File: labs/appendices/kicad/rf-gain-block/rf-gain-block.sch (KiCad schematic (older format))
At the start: 10 parts, among them P1 SMA, P2 SMA, P3 CONN_01X02, U1 ADL5602

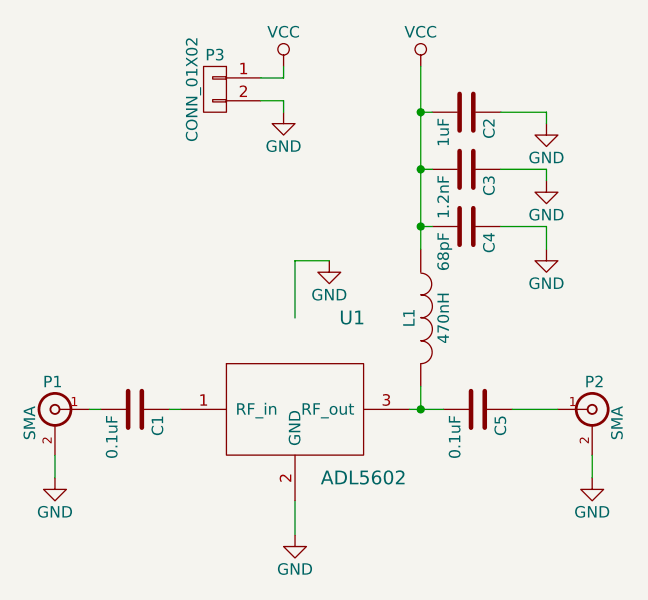
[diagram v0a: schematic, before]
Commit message: update pcb tutorial
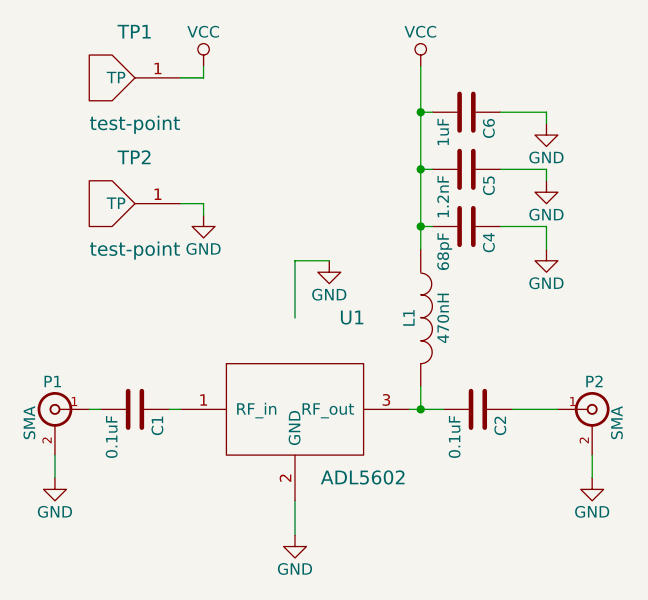
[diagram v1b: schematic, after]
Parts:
- removed P3: CONN_01X02, Pin_Headers:Pin_Header_Straight_1x02, symbol CONN_01X02
- added TP1, TP2: test-point, rf-gain-block-footprints:tp, symbol test-point
- C1, C4: footprint Capacitors_SMD:C_0402 -> rf-gain-block-footprints:smd_0603
- C2: renamed from C5; footprint Capacitors_SMD:C_0402 -> rf-gain-block-footprints:smd_0603
- C5: renamed from C3; footprint Capacitors_SMD:C_0402 -> rf-gain-block-footprints:smd_0603
- C6: renamed from C2; footprint Capacitors_SMD:C_0402 -> rf-gain-block-footprints:smd_0603
- L1: footprint (none) -> rf-gain-block-footprints:cc_0603ls
- P1, P2: footprint (none) -> rf-gain-block-footprints:SMA
- U1: footprint (none) -> rf-gain-block-footprints:adl5602
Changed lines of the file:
@@
 $EndDescr
 $Comp
-L GND #PWR4
+L GND #PWR01
 U 1 1 55D2CC7E
 P 5400 4200
-F 0 "#PWR4" H 5400 3950 50  0001 C CNN
+F 0 "#PWR01" H 5400 3950 50  0001 C CNN
 F 1 "GND" H 5400 4050 50  0000 C CNN
 F 2 "" H 5400 4200 60  0000 C CNN
@@
 F 0 "U1" H 5650 4050 60  0000 C CNN
 F 1 "ADL5602" H 5700 3350 60  0000 C CNN
-F 2 "" H 5400 3650 60  0001 C CNN
+F 2 "rf-gain-block-footprints:adl5602" H 5400 3650 60  0001 C CNN
 F 3 "" H 5400 3650 60  0000 C CNN
 	1    5400 3650
@@
 F 0 "P2" H 6710 3770 50  0000 C CNN
 F 1 "SMA" V 6810 3590 50  0000 C CNN
-F 2 "" H 6700 3650 60  0001 C CNN
+F 2 "rf-gain-block-footprints:SMA" H 6700 3650 60  0001 C CNN
 F 3 "" H 6700 3650 60  0000 C CNN
 	1    6700 3650
@@
 F 0 "P1" H 4360 3770 50  0000 C CNN
 F 1 "SMA" V 4460 3590 50  0000 C CNN
-F 2 "" H 4350 3650 60  0001 C CNN
+F 2 "rf-gain-block-footprints:SMA" H 4350 3650 60  0001 C CNN
 F 3 "" H 4350 3650 60  0000 C CNN
 	1    4350 3650
@@
 	6350 3650 6550 3650
 $Comp
-L GND #PWR10
+L GND #PWR02
 U 1 1 55D2D10F
 P 6700 3950
-F 0 "#PWR10" H 6700 3700 50  0001 C CNN
+F 0 "#PWR02" H 6700 3700 50  0001 C CNN
 F 1 "GND" H 6700 3800 50  0000 C CNN
 F 2 "" H 6700 3950 60  0000 C CNN
@@
 $EndComp
 $Comp
-L GND #PWR5
+L GND #PWR03
 U 1 1 55D2D123
 P 5550 3000
-F 0 "#PWR5" H 5550 2750 50  0001 C CNN
+F 0 "#PWR03" H 5550 2750 50  0001 C CNN
 F 1 "GND" H 5550 2850 50  0000 C CNN
 F 2 "" H 5550 3000 60  0000 C CNN
@@
 $EndComp
 $Comp
-L GND #PWR1
+L GND #PWR04
 U 1 1 55D2D137
 P 4350 3950
-F 0 "#PWR1" H 4350 3700 50  0001 C CNN
+F 0 "#PWR04" H 4350 3700 50  0001 C CNN
 F 1 "GND" H 4350 3800 50  0000 C CNN
 F 2 "" H 4350 3950 60  0000 C CNN
@@
 F 0 "C1" H 4725 3750 50  0000 L CNN
 F 1 "0.1uF" H 4725 3550 50  0000 L CNN
-F 2 "Capacitors_SMD:C_0402" H 4738 3500 30  0001 C CNN
+F 2 "rf-gain-block-footprints:smd_0603" H 4738 3500 30  0001 C CNN
 F 3 "" H 4700 3650 60  0000 C CNN
 	1    4700 3650
@@
 $EndComp
 $Comp
-L C C3
+L C C5
 U 1 1 55D2D1D7
 P 6150 2600
-F 0 "C3" H 6175 2700 50  0000 L CNN
+F 0 "C5" H 6175 2700 50  0000 L CNN
 F 1 "1.2nF" H 6175 2500 50  0000 L CNN
-F 2 "Capacitors_SMD:C_0402" H 6188 2450 30  0001 C CNN
+F 2 "rf-gain-block-footprints:smd_0603" H 6188 2450 30  0001 C CNN
 F 3 "" H 6150 2600 60  0000 C CNN
 	1    6150 2600
@@
 F 0 "C4" H 6175 2950 50  0000 L CNN
 F 1 "68pF" H 6175 2750 50  0000 L CNN
-F 2 "Capacitors_SMD:C_0402" H 6188 2700 30  0001 C CNN
+F 2 "rf-gain-block-footprints:smd_0603" H 6188 2700 30  0001 C CNN
 F 3 "" H 6150 2850 60  0000 C CNN
 	1    6150 2850
@@
 $EndComp
 $Comp
-L C C2
+L C C6
 U 1 1 55D2D25D
 P 6150 2350
-F 0 "C2" H 6175 2450 50  0000 L CNN
+F 0 "C6" H 6175 2450 50  0000 L CNN
 F 1 "1uF" H 6175 2250 50  0000 L CNN
-F 2 "Capacitors_SMD:C_0402" H 6188 2200 30  0001 C CNN
+F 2 "rf-gain-block-footprints:smd_0603" H 6188 2200 30  0001 C CNN
 F 3 "" H 6150 2350 60  0000 C CNN
 	1    6150 2350
@@
 F 0 "L1" V 5900 3250 50  0000 C CNN
 F 1 "470nH" V 6050 3250 50  0000 C CNN
-F 2 "" H 5950 3250 60  0001 C CNN
+F 2 "rf-gain-block-footprints:cc_0603ls" H 5950 3250 60  0001 C CNN
 F 3 "" H 5950 3250 60  0000 C CNN
 	1    5950 3250
@@
 $EndComp
 $Comp
-L C C5
+L C C2
 U 1 1 55D2D3C6
 P 6200 3650
-F 0 "C5" H 6225 3750 50  0000 L CNN
+F 0 "C2" H 6225 3750 50  0000 L CNN
 F 1 "0.1uF" H 6225 3550 50  0000 L CNN
-F 2 "Capacitors_SMD:C_0402" H 6238 3500 30  0001 C CNN
+F 2 "rf-gain-block-footprints:smd_0603" H 6238 3500 30  0001 C CNN
 F 3 "" H 6200 3650 60  0000 C CNN
 	1    6200 3650
@@
 	4550 3650 4500 3650
 Wire Wire Line
-	6000 2850 5950 2850
+	5950 2850 6000 2850
 Wire Wire Line
 	5950 2150 5950 2950
@@
 Connection ~ 5950 2600
 $Comp
-L GND #PWR9
+L GND #PWR05
 U 1 1 55D2D53E
 P 6500 2950
-F 0 "#PWR9" H 6500 2700 50  0001 C CNN
+F 0 "#PWR05" H 6500 2700 50  0001 C CNN
 F 1 "GND" H 6500 2800 50  0000 C CNN
 F 2 "" H 6500 2950 60  0000 C CNN
@@
 $EndComp
 $Comp
-L GND #PWR8
+L GND #PWR06
 U 1 1 55D2D576
 P 6500 2650
-F 0 "#PWR8" H 6500 2400 50  0001 C CNN
+F 0 "#PWR06" H 6500 2400 50  0001 C CNN
 F 1 "GND" H 6500 2500 50  0000 C CNN
 F 2 "" H 6500 2650 60  0000 C CNN
@@
 $EndComp
 $Comp
-L GND #PWR7
+L GND #PWR07
 U 1 1 55D2D59C
 P 6500 2400
-F 0 "#PWR7" H 6500 2150 50  0001 C CNN
+F 0 "#PWR07" H 6500 2150 50  0001 C CNN
 F 1 "GND" H 6500 2250 50  0000 C CNN
 F 2 "" H 6500 2400 60  0000 C CNN
@@
 	6500 2850 6500 2950
 $Comp
-L VCC #PWR6
+L VCC #PWR08
 U 1 1 55D2D630
 P 5950 2150
-F 0 "#PWR6" H 5950 2000 50  0001 C CNN
+F 0 "#PWR08" H 5950 2000 50  0001 C CNN
 F 1 "VCC" H 5950 2300 50  0000 C CNN
 F 2 "" H 5950 2150 60  0000 C CNN
@@
 Connection ~ 5950 2350
 $Comp
-L CONN_01X02 P3
-U 1 1 55D2DB86
-P 5050 2250
-F 0 "P3" H 5050 2400 50  0000 C CNN
-F 1 "CONN_01X02" V 5150 2250 50  0000 C CNN
-F 2 "Pin_Headers:Pin_Header_Straight_1x02" H 5050 2250 60  0001 C CNN
-F 3 "" H 5050 2250 60  0000 C CNN
-	1    5050 2250
-	-1   0    0    -1
-$EndComp
-$Comp
-L VCC #PWR2
+L VCC #PWR09
 U 1 1 55D2DC4B
-P 5350 2150
-F 0 "#PWR2" H 5350 2000 50  0001 C CNN
-F 1 "VCC" H 5350 2300 50  0000 C CNN
-F 2 "" H 5350 2150 60  0000 C CNN
-F 3 "" H 5350 2150 60  0000 C CNN
-	1    5350 2150
-	1    0    0    -1
-$EndComp
-$Comp
-L GND #PWR3
+P 5000 2150
+F 0 "#PWR09" H 5000 2000 50  0001 C CNN
+F 1 "VCC" H 5000 2300 50  0000 C CNN
+F 2 "" H 5000 2150 60  0000 C CNN
+F 3 "" H 5000 2150 60  0000 C CNN
+	1    5000 2150
+	1    0    0    -1
+$EndComp
+$Comp
+L GND #PWR010
 U 1 1 55D2DC73
-P 5350 2350
-F 0 "#PWR3" H 5350 2100 50  0001 C CNN
-F 1 "GND" H 5350 2200 50  0000 C CNN
-F 2 "" H 5350 2350 60  0000 C CNN
-F 3 "" H 5350 2350 60  0000 C CNN
-	1    5350 2350
-	1    0    0    -1
-$EndComp
-Wire Wire Line
-	5350 2150 5350 2200
-Wire Wire Line
-	5350 2200 5250 2200
-Wire Wire Line
-	5250 2300 5350 2300
-Wire Wire Line
-	5350 2300 5350 2350
+P 5000 2800
+F 0 "#PWR010" H 5000 2550 50  0001 C CNN
+F 1 "GND" H 5000 2650 50  0000 C CNN
+F 2 "" H 5000 2800 60  0000 C CNN
+F 3 "" H 5000 2800 60  0000 C CNN
+	1    5000 2800
+	1    0    0    -1
+$EndComp
+Wire Wire Line
+	5000 2150 5000 2200
+Wire Wire Line
+	5000 2200 4900 2200
+$Comp
+L test-point TP1
+U 1 1 560B7FB1
+P 4700 2200
+F 0 "TP1" H 4700 2000 60  0000 C CNN
+F 1 "test-point" H 4700 2400 60  0000 C CNN
+F 2 "rf-gain-block-footprints:tp" H 4700 2200 60  0001 C CNN
+F 3 "" H 4700 2200 60  0000 C CNN
+	1    4700 2200
+	-1   0    0    1
+$EndComp
+$Comp
+L test-point TP2
+U 1 1 560B80E2
+P 4700 2750
+F 0 "TP2" H 4700 2550 60  0000 C CNN
+F 1 "test-point" H 4700 2950 60  0000 C CNN
+F 2 "rf-gain-block-footprints:tp" H 4700 2750 60  0001 C CNN
+F 3 "" H 4700 2750 60  0000 C CNN
+	1    4700 2750
+	-1   0    0    1
+$EndComp
+Wire Wire Line
+	4900 2750 5000 2750
+Wire Wire Line
+	5000 2750 5000 2800
 $EndSCHEMATC

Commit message: update pcb tutorial
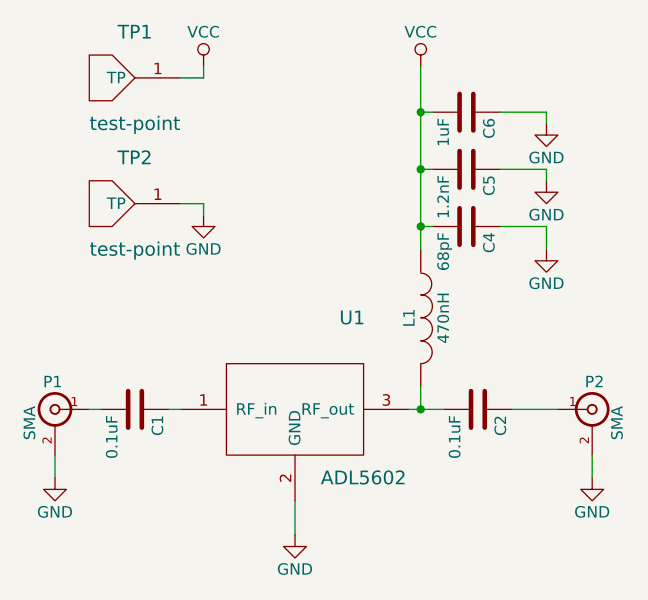
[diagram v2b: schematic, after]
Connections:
- wire segments 24 -> 22
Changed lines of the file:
@@
-$EndComp
-$Comp
-L GND #PWR03
-U 1 1 55D2D123
-P 5550 3000
-F 0 "#PWR03" H 5550 2750 50  0001 C CNN
-F 1 "GND" H 5550 2850 50  0000 C CNN
-F 2 "" H 5550 3000 60  0000 C CNN
-F 3 "" H 5550 3000 60  0000 C CNN
-	1    5550 3000
-	1    0    0    -1
 $EndComp
 $Comp
@@
 Wire Wire Line
 	6700 3950 6700 3850
-Wire Wire Line
-	5550 3000 5400 3000
-Wire Wire Line
-	5400 3000 5400 3250
 $Comp
 L C C1
